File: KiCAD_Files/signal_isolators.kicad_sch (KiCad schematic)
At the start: 24 parts, among them U801 ISO7720FDR, U802 ISO7720FDR, U803 ISO7720FDR, U804 TL431, U805 TL431, U806 TL431

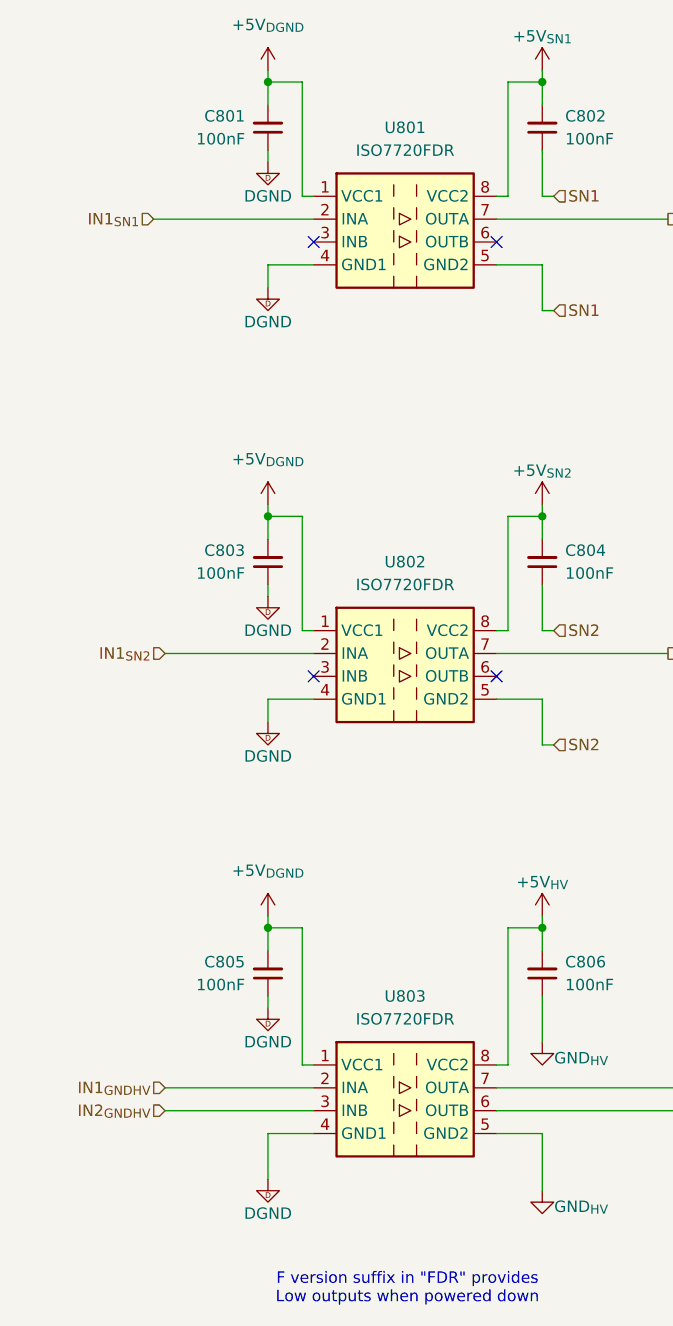
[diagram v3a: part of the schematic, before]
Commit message: Added TL431 for AC measurement 5V regulation. Added more film capacitance. Increased size of 100V ceramic caps to 1210.
Signed-off-by: Jean Alinei <jean.alinei@owntech.org>
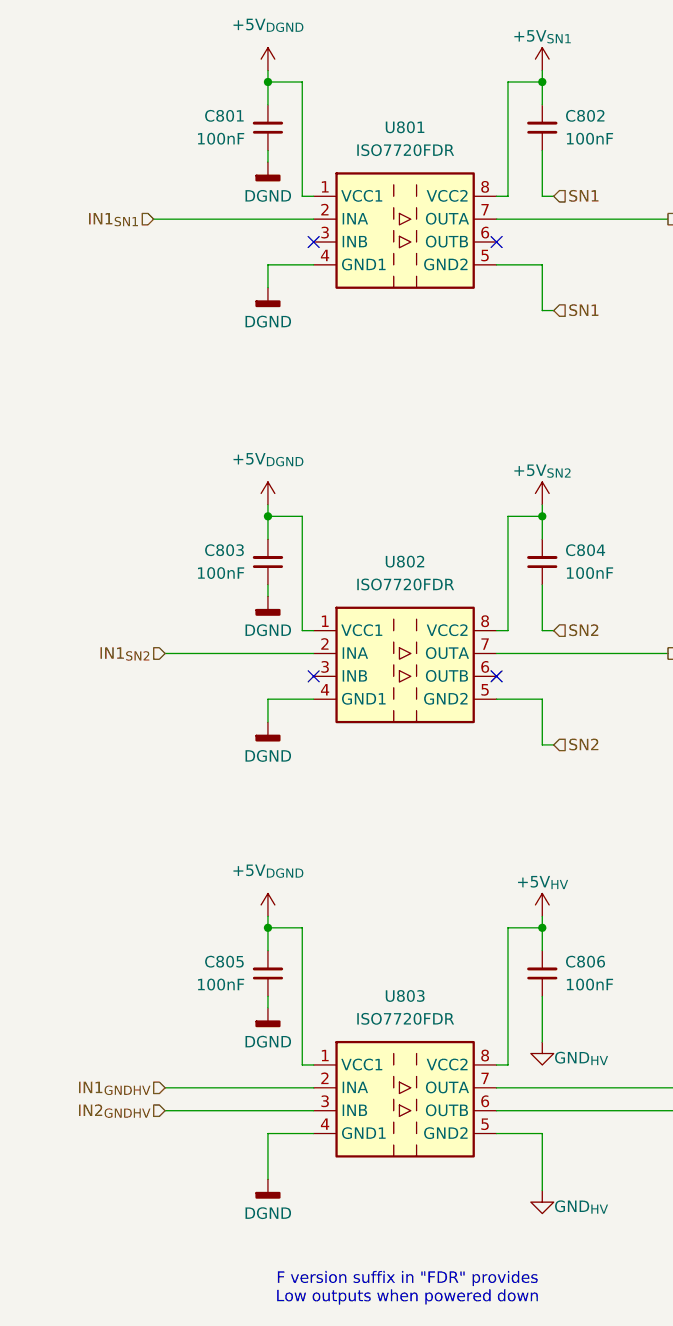
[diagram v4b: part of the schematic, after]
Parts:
- R801, R802, R803, R804, R805, R806, R807, R808, R809: footprint Capacitor_SMD:C_0805_2012Metric -> Resistor_SMD:R_0805_2012Metric
- U801, U802, U803: symbol Isolator:ISO7720DWV -> Symbols:ISO7720FDR
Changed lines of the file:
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@@
 			)
 		)
-		(property "Footprint" "Capacitor_SMD:C_0805_2012Metric"
+		(property "Footprint" "Resistor_SMD:R_0805_2012Metric"
 			(at 141.478 52.07 90)
 			(effects
@@
 	)
 	(symbol
-		(lib_id "Symbols:DGND")
+		(lib_id "power:GNDD")
 		(at 57.15 111.76 0)
 		(unit 1)
@@
 			)
 		)
-		(property "Description" ""
+		(property "Description" "Power symbol creates a global label with name \"GNDD\" , digital ground"
 			(at 57.15 111.76 0)
 			(effects
@@
 	)
 	(symbol
-		(lib_id "Symbols:+12V_PGND")
+		(lib_id "power:+12V")
 		(at 57.15 87.63 0)
 		(unit 1)
 		(exclude_from_sim no)
-		(in_bom no)
-		(on_board no)
+		(in_bom yes)
+		(on_board yes)
 		(dnp no)
 		(fields_autoplaced yes)
@@
 		)
 		(property "Footprint" ""
-			(at 60.325 85.09 0)
+			(at 57.15 87.63 0)
 			(effects
 				(font
@@
 		)
 		(property "Datasheet" ""
-			(at 60.325 85.09 0)
+			(at 57.15 87.63 0)
 			(effects
 				(font
@@
 			)
 		)
-		(property "Description" ""
+		(property "Description" "Power symbol creates a global label with name \"+12V\""
 			(at 57.15 87.63 0)
 			(effects
@@
 			)
 		)
-		(property "Footprint" "Capacitor_SMD:C_0805_2012Metric"
+		(property "Footprint" "Resistor_SMD:R_0805_2012Metric"
 			(at 141.478 143.51 90)
 			(effects
@@
 	)
 	(symbol
-		(lib_id "Isolator:ISO7720DWV")
+		(lib_id "Symbols:ISO7720FDR")
 		(at 72.39 58.42 0)
 		(unit 1)
@@
 	)
 	(symbol
-		(lib_id "Symbols:DGND")
+		(lib_id "power:GNDD")
 		(at 57.15 49.53 0)
 		(unit 1)
@@
 			)
 		)
-		(property "Description" ""
+		(property "Description" "Power symbol creates a global label with name \"GNDD\" , digital ground"
 			(at 57.15 49.53 0)
 			(effects
@@
 			)
 		)
-		(property "Footprint" "Capacitor_SMD:C_0805_2012Metric"
+		(property "Footprint" "Resistor_SMD:R_0805_2012Metric"
 			(at 141.478 110.49 90)
 			(effects
@@
 			)
 		)
-		(property "Footprint" "Capacitor_SMD:C_0805_2012Metric"
+		(property "Footprint" "Resistor_SMD:R_0805_2012Metric"
 			(at 129.54 93.472 90)
 			(effects
@@
 			)
 		)
-		(property "Footprint" "Capacitor_SMD:C_0805_2012Metric"
+		(property "Footprint" "Resistor_SMD:R_0805_2012Metric"
 			(at 141.478 153.67 90)
 			(effects
@@
 	)
 	(symbol
-		(lib_id "Symbols:DGND")
+		(lib_id "power:GNDD")
 		(at 57.15 63.5 0)
 		(unit 1)
@@
 			)
 		)
-		(property "Description" ""
+		(property "Description" "Power symbol creates a global label with name \"GNDD\" , digital ground"
 			(at 57.15 63.5 0)
 			(effects
@@
 	)
 	(symbol
-		(lib_id "Symbols:+12V_PGND")
+		(lib_id "power:+12V")
 		(at 57.15 133.35 0)
 		(unit 1)
 		(exclude_from_sim no)
-		(in_bom no)
-		(on_board no)
+		(in_bom yes)
+		(on_board yes)
 		(dnp no)
 		(fields_autoplaced yes)
@@
 		)
 		(property "Footprint" ""
-			(at 60.325 130.81 0)
+			(at 57.15 133.35 0)
 			(effects
 				(font
@@
 		)
 		(property "Datasheet" ""
-			(at 60.325 130.81 0)
+			(at 57.15 133.35 0)
 			(effects
 				(font
@@
 			)
 		)
-		(property "Description" ""
+		(property "Description" "Power symbol creates a global label with name \"+12V\""
 			(at 57.15 133.35 0)
 			(effects
@@
 			)
 		)
-		(property "Footprint" "Capacitor_SMD:C_0805_2012Metric"
+		(property "Footprint" "Resistor_SMD:R_0805_2012Metric"
 			(at 129.54 136.652 90)
 			(effects
@@
 	)
 	(symbol
-		(lib_id "Symbols:DGND")
+		(lib_id "power:GNDD")
 		(at 57.15 143.51 0)
 		(unit 1)
@@
 			)
 		)
-		(property "Description" ""
+		(property "Description" "Power symbol creates a global label with name \"GNDD\" , digital ground"
 			(at 57.15 143.51 0)
 			(effects
@@
 	)
 	(symbol
-		(lib_id "Isolator:ISO7720DWV")
+		(lib_id "Symbols:ISO7720FDR")
 		(at 72.39 154.94 0)
 		(unit 1)
@@
 	)
 	(symbol
-		(lib_id "Isolator:ISO7720DWV")
+		(lib_id "Symbols:ISO7720FDR")
 		(at 72.39 106.68 0)
 		(unit 1)
@@
 	)
 	(symbol
-		(lib_id "Symbols:DGND")
+		(lib_id "power:GNDD")
 		(at 57.15 97.79 0)
 		(unit 1)
@@
 			)
 		)
-		(property "Description" ""
+		(property "Description" "Power symbol creates a global label with name \"GNDD\" , digital ground"
 			(at 57.15 97.79 0)
 			(effects
@@
 			)
 		)
-		(property "Footprint" "Capacitor_SMD:C_0805_2012Metric"
+		(property "Footprint" "Resistor_SMD:R_0805_2012Metric"
 			(at 129.54 45.212 90)
 			(effects
@@
 	)
 	(symbol
-		(lib_id "Symbols:DGND")
+		(lib_id "power:GNDD")
 		(at 57.15 162.56 0)
 		(unit 1)
@@
 			)
 		)
-		(property "Description" ""
+		(property "Description" "Power symbol creates a global label with name \"GNDD\" , digital ground"
 			(at 57.15 162.56 0)
 			(effects
@@
 	)
 	(symbol
-		(lib_id "Symbols:+12V_PGND")
+		(lib_id "power:+12V")
 		(at 57.15 39.37 0)
 		(unit 1)
 		(exclude_from_sim no)
-		(in_bom no)
-		(on_board no)
+		(in_bom yes)
+		(on_board yes)
 		(dnp no)
 		(fields_autoplaced yes)
@@
 		)
 		(property "Footprint" ""
-			(at 60.325 36.83 0)
+			(at 57.15 39.37 0)
 			(effects
 				(font
@@
 		)
 		(property "Datasheet" ""
-			(at 60.325 36.83 0)
+			(at 57.15 39.37 0)
 			(effects
 				(font
@@
 			)
 		)
-		(property "Description" ""
+		(property "Description" "Power symbol creates a global label with name \"+12V\""
 			(at 57.15 39.37 0)
 			(effects
@@
 			)
 		)
-		(property "Footprint" "Capacitor_SMD:C_0805_2012Metric"
+		(property "Footprint" "Resistor_SMD:R_0805_2012Metric"
 			(at 141.478 62.23 90)
 			(effects
@@
 			)
 		)
-		(property "Footprint" "Capacitor_SMD:C_0805_2012Metric"
+		(property "Footprint" "Resistor_SMD:R_0805_2012Metric"
 			(at 141.478 100.33 90)
 			(effects

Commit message: Tidied up the schematic. Added the pdf version for V0.9.
Signed-off-by: Jean Alinei <jean.alinei@owntech.org>
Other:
- title: (none) -> Inverter PWM isolators
- moved on the sheet: C801, C802, C803, C804, C805, C806, C807, C808, C809, R801, R802, R803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
